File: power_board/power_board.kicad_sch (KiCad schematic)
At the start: 59 parts, among them J1 Conn_01x02_Pin, J2 I2C, J3 12V_Out, Q1 NTMFS5C430NLT1G, SW1 SW_SPDT, U1 TPS54560BDDA, U2 TPS54560BDDA, U3 ADC081C021CIMM

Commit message: feat: 10A converters
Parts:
- removed C1: 2.2u, Capacitor_SMD:C_0805_2012Metric, symbol Device:C
- removed C19, C20: 47u, Capacitor_SMD:C_1206_3216Metric, symbol Device:C
- removed D1, D2: B560C, Diode_SMD:D_SMC, symbol Device:D_Schottky
- removed R10: 26.1k, Resistor_SMD:R_0805_2012Metric, symbol Device:R
- removed R11: 140k, Resistor_SMD:R_0805_2012Metric, symbol Device:R
- removed R12: 10k, Resistor_SMD:R_0805_2012Metric, symbol Device:R
- removed R9: 243k, Resistor_SMD:R_0805_2012Metric, symbol Device:R
- removed U1, U2: TPS54560BDDA, Package_SO:Texas_R-PDSO-G8_EP2.95x4.9mm_Mask2.4x3.1mm_ThermalVias, symbol Regulator_Switching:TPS54560BDDA
- added J2: Conn_01x02_Socket, Connector_AMASS:AMASS_XT30PW-F_1x02_P2.50mm_Horizontal, symbol Connector:Conn_01x02_Socket
- added NT1: NetTie_2, NetTie:NetTie-2_SMD_Pad0.5mm, symbol Device:NetTie_2
- added U1, U2: TPS56A37RPAR, RPA0010A-MFG, symbol TPS56A37RPAR:TPS56A37RPAR
- C10, C8, C9: value 47u -> 22u; footprint Capacitor_SMD:C_1206_3216Metric -> Capacitor_SMD:C_0805_2012Metric; LCSC C6119972 -> C7419435
- C11: value 2.2u -> 22u; LCSC C2903667 -> C7419435
- C12, C14, C4: value 2.2u -> 100n; LCSC C2903667 -> C5137467
- C13: value 2.2u -> 22n; LCSC C2903667 -> C5137639
- C15: value 100n -> 33p; LCSC C476766 -> C7419432
- C16: value 8.2n -> 10u; LCSC C296107 -> C5137488
- C17: value 30p -> 10u; LCSC C22399636 -> C5137488
- C18: value 47u -> 10u; footprint Capacitor_SMD:C_1206_3216Metric -> Capacitor_SMD:C_0805_2012Metric; LCSC C6119972 -> C5137488
- C2, C3: value 2.2u -> 10u; LCSC C2903667 -> C5137488
- C5: value 100n -> 22n; LCSC C476766 -> C5137639
- C6: value 4.7n -> 100n; LCSC C5375827 -> C5137467
- C7: value 47p -> 150p; LCSC C22399638 -> C7467159
- J3: value 12V_Out -> Conn_01x02_Socket
- L1: value 10u -> 3.3u; footprint Inductor_SMD:L_TechFuse_SL1250 -> Inductor_SMD:L_APV_APH1030; LCSC C22463852 -> C845075
- L2: value 22u -> 6.8u; footprint Inductor_SMD:L_TechFuse_SL1250 -> Inductor_SMD:L_TaiTech_TMPC1265_13.5x12.5mm; LCSC C22463853 -> C2847562
- R1: value 150k -> 115k; LCSC C2907228 -> C2933289
- R2, R8: value 15k -> 10k; LCSC C2930170 -> C2907219
- R3: value 243k -> 52.3k; LCSC C2930186 -> C2933465
- R4: value 16.9k -> 73.2k; LCSC C2933336 -> C5713314
- R5: value 52.3k -> 10k; LCSC C2933465 -> C2907219
- R6: value 10k -> 52.3k; LCSC C2907219 -> C2933465
- R7: value 150k -> 191k; LCSC C2907228 -> C3000728
- renumbered C23 to C1, C21 to C19, C22 to C20, D3 to D1, J2 to J4, R14 to R10, R15 to R11, R16 to R12, R17 to R13, R18 to R14, R19 to R15, R13 to R9
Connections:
- net +12V: now also C15.1, C16.1, C17.1, R7.1
- net +5V: now also C7.1, R4.1, J2.1 (Pin_1); no longer C10.1
- net +BATT: now also C10.1, U1.8 (VIN), U2.8 (VIN); no longer C13.1, C14.1, R7.1
- net AGND: now reaches C5.2
- net AGND: now also C13.2, R2.2, R3.2, R5.2, R6.2, R8.2, NT1.1, U1.3 (AGND), U2.3 (AGND)
- net EN: now reaches R1.2, R2.1
- net EN: now also U1.1 (EN), U2.1 (EN)
- net at R3.1: now also U1.10 (MODE)
- net at R6.1: now also U2.10 (MODE); no longer R5.2
- net at R4.2: now also C7.2, R5.1, U1.2 (FB); no longer C6.1
- net at R7.2, R8.1: now also C15.2, U2.2 (FB)
- net at L2.1: now also C14.1, U2.6 (SW); no longer C15.1
- net GND renamed PGND
- net PGND: now also J2.2 (Pin_2), NT1.2, U1.9 (PGND), U2.9 (PGND); no longer C13.2, C14.2, C6.2, C7.2, R2.2, R3.2, R6.2, R8.2
- new net: C13.1, U2.5 (SS)
- new net: C14.2, U2.7 (BOOT)
- new net: C6.1, L1.1, U1.6 (SW)
- new net: C5.1, U1.5 (SS)
- new net: C6.2, U1.7 (BOOT)
- no-connect marks 1 -> 3
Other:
- note added: "12V Buck Converter"
- note added: "5V Buck Converter"
- note added: "Enable logic low is 1.07V Desired cutoff battery voltage is 13.5V"
- note removed: "12V Buck with UVLO"
- note removed: "5V Buck with UVLO"
- note removed: "C6"
- note removed: "C7"
- note removed: "Min inductance is 16u This is a rather overkill 7A inductor but it has only 39.5m resistance"
- note removed: "Min inductance is 7.6u This is a rather overkill 10A inductor but it has only 18m resistance"
- note removed: "VStart = 13.5V VStop = 13V IHys = 3.4uA I1 = 1.2uA VEna = 1.2V"
- note removed: "fPmod = 759 Hz fZmod = 1100 kHz fco1 = 28.9 kHz fco2 = 12.3 kHz fco = sqrt(fco1*fco2) = 18.9 kHz R10 = 26.2k C16 = 8n C17 = 30p"
- moved on the sheet: C1, C19, C20, D1, H1, H2, H3, H4, J1, J3, J4, Q1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

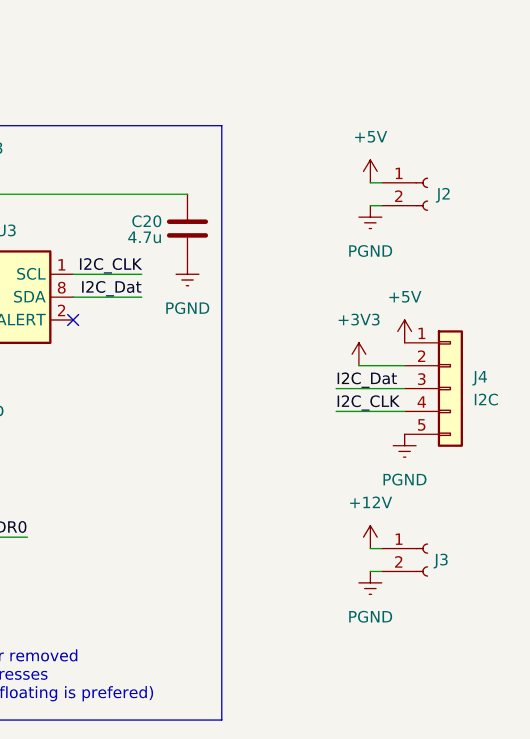
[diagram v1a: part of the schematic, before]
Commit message: larger power traces
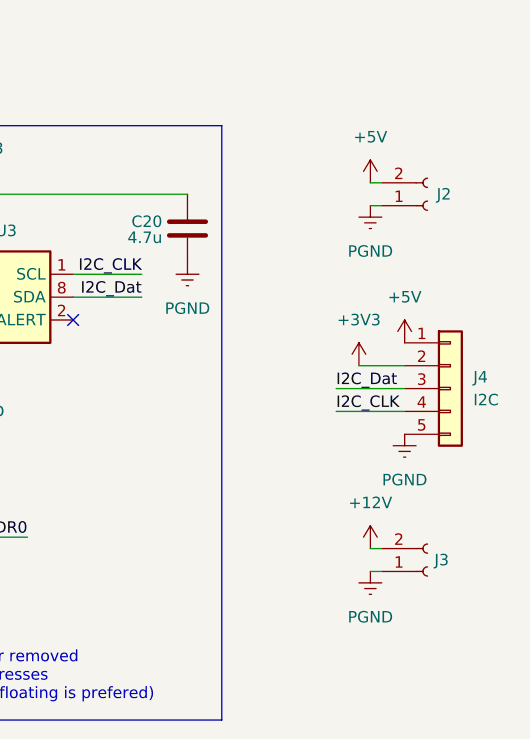
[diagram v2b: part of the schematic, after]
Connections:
- net +12V: now also J3.2 (Pin_2); no longer J3.1 (Pin_1)
- net +5V: now also J2.2 (Pin_2); no longer J2.1 (Pin_1)
- net PGND: now also J2.1 (Pin_1), J3.1 (Pin_1); no longer J2.2 (Pin_2), J3.2 (Pin_2)
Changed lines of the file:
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@@
 	(symbol
 		(lib_id "Connector:Conn_01x02_Socket")
-		(at 250.19 58.42 0)
+		(at 250.19 60.96 0)
+		(mirror x)
 		(unit 1)
 		(exclude_from_sim no)
@@
 		)
 		(property "Value" "Conn_01x02_Socket"
-			(at 251.46 60.9599 0)
+			(at 251.46 58.4201 0)
 			(effects
 				(font
@@
 		)
 		(property "Footprint" "Connector_AMASS:AMASS_XT30PW-F_1x02_P2.50mm_Horizontal"
-			(at 250.19 58.42 0)
+			(at 250.19 60.96 0)
 			(effects
 				(font
@@
 		)
 		(property "Datasheet" "~"
-			(at 250.19 58.42 0)
+			(at 250.19 60.96 0)
 			(effects
 				(font
@@
 		)
 		(property "Description" "Generic connector, single row, 01x02, script generated"
-			(at 250.19 58.42 0)
+			(at 250.19 60.96 0)
 			(effects
 				(font
@@
 		)
 		(property "LCSC" "C2913282"
-			(at 250.19 58.42 0)
+			(at 250.19 60.96 0)
 			(effects
 				(font
@@
 	(symbol
 		(lib_id "Connector:Conn_01x02_Socket")
-		(at 250.19 99.06 0)
+		(at 250.19 101.6 0)
+		(mirror x)
 		(unit 1)
 		(exclude_from_sim no)
@@
 		)
 		(property "Value" "Conn_01x02_Socket"
-			(at 251.46 101.5999 0)
+			(at 251.46 99.0601 0)
 			(effects
 				(font
@@
 		)
 		(property "Footprint" "Connector_AMASS:AMASS_XT30PW-F_1x02_P2.50mm_Horizontal"
-			(at 250.19 99.06 0)
+			(at 250.19 101.6 0)
 			(effects
 				(font
@@
 		)
 		(property "Datasheet" "~"
-			(at 250.19 99.06 0)
+			(at 250.19 101.6 0)
 			(effects
 				(font
@@
 		)
 		(property "Description" "Generic connector, single row, 01x02, script generated"
-			(at 250.19 99.06 0)
+			(at 250.19 101.6 0)
 			(effects
 				(font
@@
 		)
 		(property "LCSC" "C2913282"
-			(at 250.19 99.06 0)
+			(at 250.19 101.6 0)
 			(effects
 				(font
@@
 		)
 		(instances
-			(project ""
+			(project "power_board"
 				(path "/6c81df62-f6a4-49c0-94c7-8d27709f5562"
 					(reference "J3")
